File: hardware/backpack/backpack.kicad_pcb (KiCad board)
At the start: 2 copper layers, 31.7 x 110 mm, 99 parts, among them J1 Conn_01x15, J2 Conn_02x06_Top_Bottom, J3 Conn_02x06_Top_Bottom, J4 AUDIO JACK PJ-324M0, J5 AUDIO JACK PJ-324M0, J6 CONN 2x5 P=2.54mm, J7 USB_C, J8 MICROMOD-2222, J9 USB_C, Q2 2N7002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

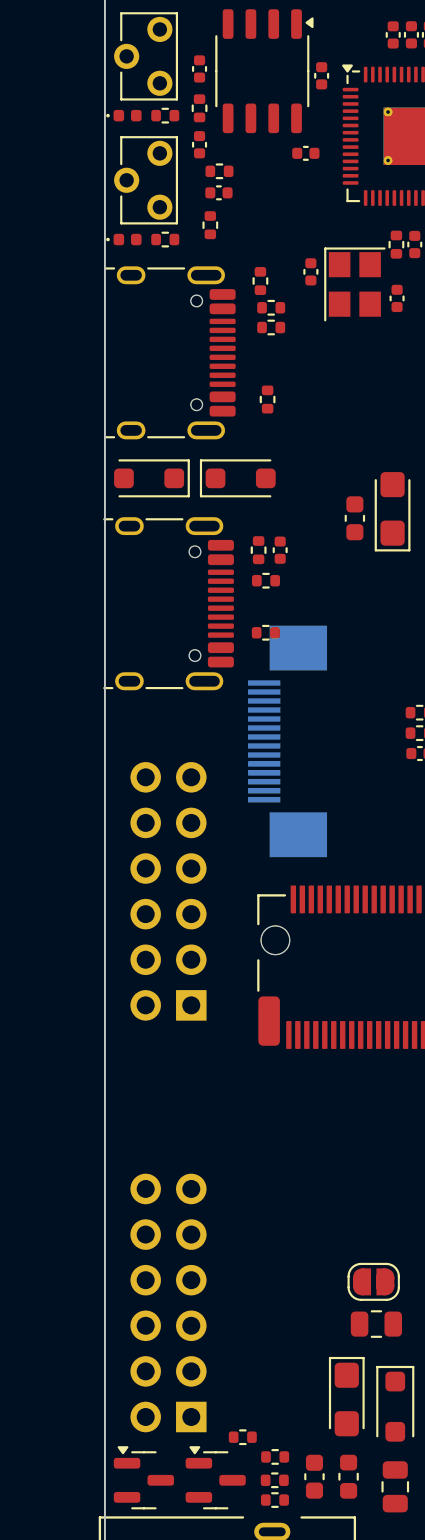
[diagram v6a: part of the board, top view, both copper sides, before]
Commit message: fix pmod spacing
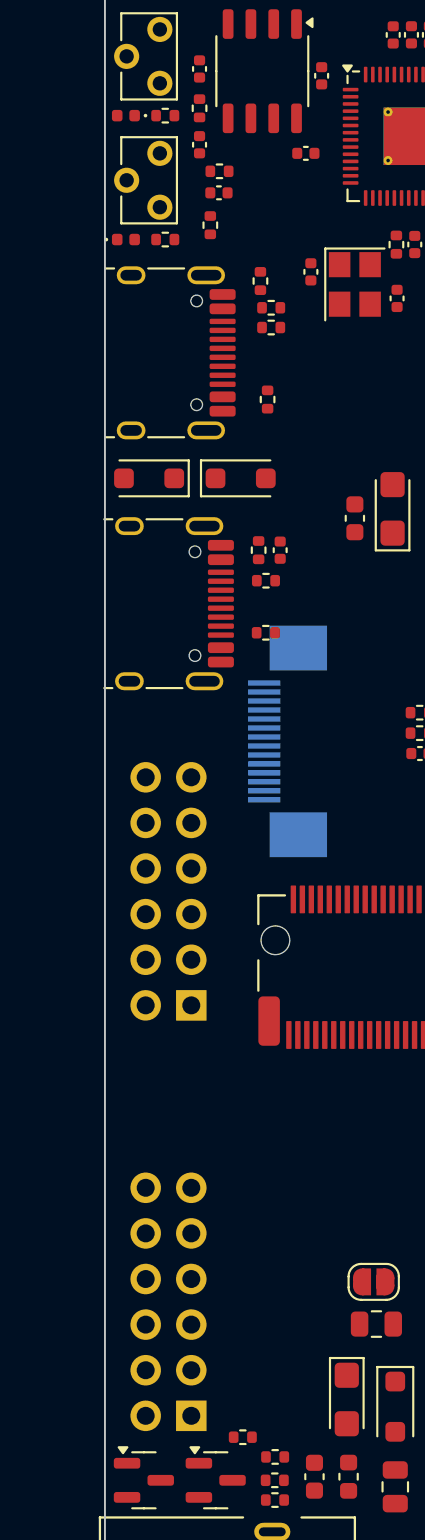
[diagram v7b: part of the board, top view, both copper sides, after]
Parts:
- moved D8 0.09 mm to (1.10, 18.5), turned to 180 degrees
- moved D9 0.09 mm to (1.10, 25.4)
- moved J2 0.07 mm to (4.74, 78.2)
- turned R29 to 180 degrees
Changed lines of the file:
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@@
 		(pad_to_mask_clearance 0)
 		(allow_soldermask_bridges_in_footprints no)
+		(grid_origin 4.74 55.35)
 		(pcbplotparams
 			(layerselection 0x00010fc_ffffffff)
@@
 	(footprint "Resistor_SMD:R_0402_1005Metric"
 		(layer "F.Cu")
-		(at 3.29 18.5)
+		(at 3.29 18.5 180)
 		(descr "Resistor SMD 0402 (1005 Metric), square (rectangular) end terminal, IPC_7351 nominal, (Body size source: IPC-SM-782 page 72, https://www.pcb-3d.com/wordpress/wp-content/uploads/ipc-sm-782a_amendment_1_and_2.pdf), generated with kicad-footprint-generator")
 		(tags "resistor")
 		(property "Reference" "R29"
-			(at 0 -1.17 0)
+			(at 0 -1.17 180)
 			(layer "F.SilkS")
 			(hide yes)
@@
 		)
 		(property "Value" "100R/R0402"
-			(at 0 1.17 0)
+			(at 0 1.17 180)
 			(layer "F.Fab")
 			(effects
@@
 		)
 		(property "Footprint" "Resistor_SMD:R_0402_1005Metric"
-			(at 0 0 0)
+			(at 0 0 180)
 			(unlocked yes)
 			(layer "F.Fab")
@@
 		)
 		(property "Datasheet" ""
-			(at 0 0 0)
+			(at 0 0 180)
 			(unlocked yes)
 			(layer "F.Fab")
@@
 		)
 		(property "Description" ""
-			(at 0 0 0)
+			(at 0 0 180)
 			(unlocked yes)
 			(layer "F.Fab")
@@
 		)
 		(property "lcsc#" "  C106232"
-			(at 0 0 0)
+			(at 0 0 180)
 			(unlocked yes)
 			(layer "F.Fab")
@@
 		(attr smd)
 		(fp_line
-			(start -0.153641 -0.38)
-			(end 0.153641 -0.38)
+			(start -0.153641 0.38)
+			(end 0.153641 0.38)
 			(stroke
 				(width 0.12)
@@
 		)
 		(fp_line
-			(start -0.153641 0.38)
-			(end 0.153641 0.38)
+			(start -0.153641 -0.38)
+			(end 0.153641 -0.38)
 			(stroke
 				(width 0.12)
@@
 		)
 		(fp_line
-			(start -0.93 -0.47)
-			(end 0.93 -0.47)
+			(start 0.93 0.47)
+			(end -0.93 0.47)
 			(stroke
 				(width 0.05)
@@
 		)
 		(fp_line
-			(start -0.93 0.47)
-			(end -0.93 -0.47)
+			(start 0.93 -0.47)
+			(end 0.93 0.47)
 			(stroke
 				(width 0.05)
@@
 		)
 		(fp_line
-			(start 0.93 -0.47)
-			(end 0.93 0.47)
+			(start -0.93 0.47)
+			(end -0.93 -0.47)
 			(stroke
 				(width 0.05)
@@
 		)
 		(fp_line
-			(start 0.93 0.47)
-			(end -0.93 0.47)
+			(start -0.93 -0.47)
+			(end 0.93 -0.47)
 			(stroke
 				(width 0.05)
@@
 		)
 		(fp_line
-			(start -0.525 -0.27)
-			(end 0.525 -0.27)
+			(start 0.525 0.27)
+			(end -0.525 0.27)
 			(stroke
 				(width 0.1)
@@
 		)
 		(fp_line
-			(start -0.525 0.27)
-			(end -0.525 -0.27)
+			(start 0.525 -0.27)
+			(end 0.525 0.27)
 			(stroke
 				(width 0.1)
@@
 		)
 		(fp_line
-			(start 0.525 -0.27)
-			(end 0.525 0.27)
+			(start -0.525 0.27)
+			(end -0.525 -0.27)
 			(stroke
 				(width 0.1)
@@
 		)
 		(fp_line
-			(start 0.525 0.27)
-			(end -0.525 0.27)
+			(start -0.525 -0.27)
+			(end 0.525 -0.27)
 			(stroke
 				(width 0.1)
@@
 		)
 		(fp_text user "${REFERENCE}"
-			(at 0 0 0)
+			(at 0 0 180)
 			(layer "F.Fab")
 			(effects
@@
 		)
 		(pad "1" smd roundrect
-			(at -0.51 0)
+			(at -0.51 0 180)
 			(size 0.54 0.64)
 			(layers "F.Cu" "F.Paste" "F.Mask")
@@
 		)
 		(pad "2" smd roundrect
-			(at 0.51 0)
+			(at 0.51 0 180)
 			(size 0.54 0.64)
 			(layers "F.Cu" "F.Paste" "F.Mask")
@@
 	(footprint "LED_SMD:LED_0402_1005Metric"
 		(layer "F.Cu")
-		(at 1.19 18.5)
+		(at 1.1 18.5 180)
 		(descr "LED SMD 0402 (1005 Metric), square (rectangular) end terminal, IPC_7351 nominal, (Body size source: http://www.tortai-tech.com/upload/download/2011102023233369053.pdf), generated with kicad-footprint-generator")
 		(tags "LED")
 		(property "Reference" "D8"
-			(at 0 -1.17 0)
+			(at 0 -1.17 180)
 			(layer "F.SilkS")
 			(hide yes)
@@
 		)
 		(property "Value" "LED 0402 RED"
-			(at 0 1.17 0)
+			(at 0 1.17 180)
 			(layer "F.Fab")
 			(effects
@@
 		)
 		(property "Footprint" "LED_SMD:LED_0402_1005Metric"
-			(at 0 0 0)
+			(at 0 0 180)
 			(unlocked yes)
 			(layer "F.Fab")
@@
 		)
 		(property "Datasheet" ""
-			(at 0 0 0)
+			(at 0 0 180)
 			(unlocked yes)
 			(layer "F.Fab")
@@
 		)
 		(property "Description" "Light emitting diode, small symbol, filled shape"
-			(at 0 0 0)
+			(at 0 0 180)
 			(unlocked yes)
 			(layer "F.Fab")
@@
 		)
 		(property "lcsc#" "C965790"
-			(at 0 0 0)
+			(at 0 0 180)
 			(unlocked yes)
 			(layer "F.Fab")
@@
 		)
 		(fp_line
-			(start -0.93 -0.47)
-			(end 0.93 -0.47)
+			(start 0.93 0.47)
+			(end -0.93 0.47)
 			(stroke
 				(width 0.05)
@@
 		)
 		(fp_line
-			(start -0.93 0.47)
-			(end -0.93 -0.47)
+			(start 0.93 -0.47)
+			(end 0.93 0.47)
 			(stroke
 				(width 0.05)
@@
 		)
 		(fp_line
-			(start 0.93 -0.47)
-			(end 0.93 0.47)
+			(start -0.93 0.47)
+			(end -0.93 -0.47)
 			(stroke
 				(width 0.05)
@@
 		)
 		(fp_line
-			(start 0.93 0.47)
-			(end -0.93 0.47)
+			(start -0.93 -0.47)
+			(end 0.93 -0.47)
 			(stroke
 				(width 0.05)
@@
 		)
 		(fp_line
-			(start -0.5 -0.25)
-			(end 0.5 -0.25)
+			(start 0.5 0.25)
+			(end -0.5 0.25)
 			(stroke
 				(width 0.1)
@@
 		)
 		(fp_line
-			(start -0.5 0.25)
-			(end -0.5 -0.25)
+			(start 0.5 -0.25)
+			(end 0.5 0.25)
 			(stroke
 				(width 0.1)
@@
 		)
 		(fp_line
-			(start -0.4 0.25)
-			(end -0.4 -0.25)
+			(start -0.3 0.25)
+			(end -0.3 -0.25)
 			(stroke
 				(width 0.1)
@@
 		)
 		(fp_line
-			(start -0.3 0.25)
-			(end -0.3 -0.25)
+			(start -0.4 0.25)
+			(end -0.4 -0.25)
 			(stroke
 				(width 0.1)
@@
 		)
 		(fp_line
-			(start 0.5 -0.25)
-			(end 0.5 0.25)
+			(start -0.5 0.25)
+			(end -0.5 -0.25)
 			(stroke
 				(width 0.1)
@@
 		)
 		(fp_line
-			(start 0.5 0.25)
-			(end -0.5 0.25)
+			(start -0.5 -0.25)
+			(end 0.5 -0.25)
 			(stroke
 				(width 0.1)
@@
 		)
 		(fp_text user "${REFERENCE}"
-			(at 0 0 0)
+			(at 0 0 180)
 			(layer "F.Fab")
 			(effects
@@
 		)
 		(pad "1" smd roundrect
-			(at -0.485 0)
+			(at -0.485 0 180)
 			(size 0.59 0.64)
 			(layers "F.Cu" "F.Paste" "F.Mask")
@@
 		)
 		(pad "2" smd roundrect
-			(at 0.485 0)
+			(at 0.485 0 180)
 			(size 0.59 0.64)
 			(layers "F.Cu" "F.Paste" "F.Mask")
@@
 	(footprint "LED_SMD:LED_0402_1005Metric"
 		(layer "F.Cu")
-		(at 1.19 25.4)
+		(at 1.1 25.4)
 		(descr "LED SMD 0402 (1005 Metric), square (rectangular) end terminal, IPC_7351 nominal, (Body size source: http://www.tortai-tech.com/upload/download/2011102023233369053.pdf), generated with kicad-footprint-generator")
 		(tags "LED")
 		(property "Reference" "D9"
-			(at 0 -1.17 0)
+			(at 0 -1.17 360)
 			(layer "F.SilkS")
 			(hide yes)
@@
 		)
 		(property "Value" "LED 0402 RED"
-			(at 0 1.17 0)
+			(at 0 1.17 360)
 			(layer "F.Fab")
 			(effects
@@
 		)
 		(fp_text user "${REFERENCE}"
-			(at 0 0 0)
+			(at 0 0 360)
 			(layer "F.Fab")
 			(effects
@@
 	(footprint "Connector_PinSocket_2.54mm:PinSocket_2x06_P2.54mm_Horizontal"
 		(layer "F.Cu")
-		(at 4.74 78.275)
+		(at 4.74 78.21)
 		(descr "Through hole angled socket strip, 2x06, 2.54mm pitch, 8.51mm socket length, double cols (from Kicad 4.0.7), script generated")
 		(tags "Through hole angled socket strip THT 2x06 2.54mm double row")
@@
 		(tags "resistor")
 		(property "Reference" "R30"
-			(at 0 -1.17 0)
+			(at 0 -1.17 360)
 			(layer "F.SilkS")
 			(hide yes)
@@
 		)
 		(property "Value" "100R/R0402"
-			(at 0 1.17 0)
+			(at 0 1.17 360)
 			(layer "F.Fab")
 			(effects
@@
 		)
 		(fp_text user "${REFERENCE}"
-			(at 0 0 0)
+			(at 0 0 360)
 			(layer "F.Fab")
 			(effects
@@
 		(layer "Dwgs.User")
 		(pts
-			(xy 5.24 68.075) (xy 5.25 78.25)
+			(xy 4.74 68.05) (xy 4.74 78.21)
 		)
 		(height 21.149052)
-		(gr_text "10.1750 mm"
-			(at -14.754043 73.182155 270.0563103)
+		(gr_text "10.1600 mm"
+			(at -17.559052 73.13 90)
 			(layer "Dwgs.User")
 			(effects

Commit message: routing done
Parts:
- moved C14 0.96 mm to (15.5, 13.2)
- moved C17 0.70 mm to (6.28, 23.5)
- moved R3 0.55 mm to (5.80, 25.1)
- moved R8 0.55 mm to (6.31, 22.1)
- moved C9 0.25 mm to (18.0, 13.8)
- turned D9 to 180 degrees
- turned R1 to 90 degrees
- turned R26 to 180 degrees
- turned R30 to 180 degrees
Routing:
- net ECP5_A7: track 0.00 -> 78.4 mm, vias 0 -> 4
- net ECP5_A3: track 0.00 -> 74.7 mm, vias 0 -> 4
- net ECP5_C4: track 0.00 -> 67.0 mm, vias 0 -> 4
- net ECP5_B7: track 0.00 -> 65.1 mm, vias 0 -> 2
- net GND: track 0.00 -> 61.4 mm, vias 0 -> 28
- net +3V3: track 0.00 -> 60.9 mm, vias 0 -> 24
- net ECP5_B4: track 0.00 -> 58.6 mm, vias 0 -> 6
- net ECP5_A4: track 0.00 -> 58.5 mm, vias 0 -> 6
- net ECP5_D5: track 0.00 -> 58.0 mm, vias 0 -> 2
- net ECP5_T11_TMS: track 0.00 -> 57.5 mm, vias 0 -> 2
- net ECP5_M10_TDO: track 0.00 -> 56.5 mm, vias 0 -> 2
- net +12V: track 0.00 -> 55.2 mm, vias 0 -> 2
- net Net-(D4-K): track 0.00 -> 53.9 mm, vias 0 -> 2
- net -12V: track 0.00 -> 51.8 mm, vias 0 -> 2
- net +2V5: track 0.00 -> 50.8 mm, vias 0 -> 5
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- added copper zone on In1.Cu, net +3V3
- added copper zone on B.Cu, net GND
- added copper zone on F.Cu, net GND
- added copper zone on In2.Cu, net GND
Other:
- copper layers 2 -> 4
- board text added: "LOGIKEET"
- board text added: "proto1"
